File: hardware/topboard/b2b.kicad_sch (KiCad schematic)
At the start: 50 parts

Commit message: Add IMU
Signed-off-by: gatecat <gatecat@ds0.me>
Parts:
- removed C? (x4): 100n, symbol Device:C_Small
- added C? (x4): 100n, symbol Device:C_Small
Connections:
- net GTR_LEFT_C2M+: now also JL.B20
- net GTR_LEFT_C2M-: now also JL.B21
- net GTR_LEFT_M2C+: now also JL.B23
- net GTR_LEFT_M2C-: now also JL.B24
- net GTR_RIGHT_C2M+: now also C?.2; no longer JL?.B23
- net GTR_RIGHT_C2M-: now also C?.2; no longer JL?.B24
- net GTR_RIGHT_M2C+: now also C?.2; no longer JL?.B20
- net GTR_RIGHT_M2C-: now also C?.2; no longer JL?.B21
- new net: C?.1, JL?.B20
- new net: C?.1, JL?.B21
- new net: C?.1, JL?.B23
- new net: C?.1, JL?.B24

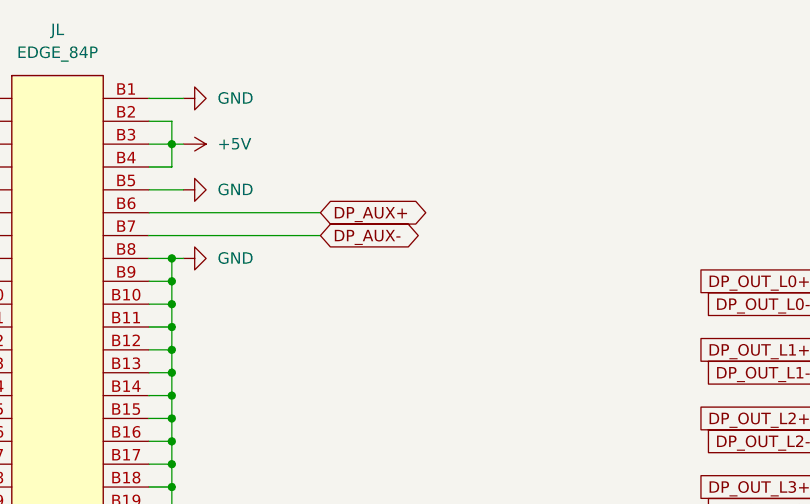
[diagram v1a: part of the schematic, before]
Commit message: Connecting some misc SoM IO
Signed-off-by: gatecat <gatecat@ds0.me>
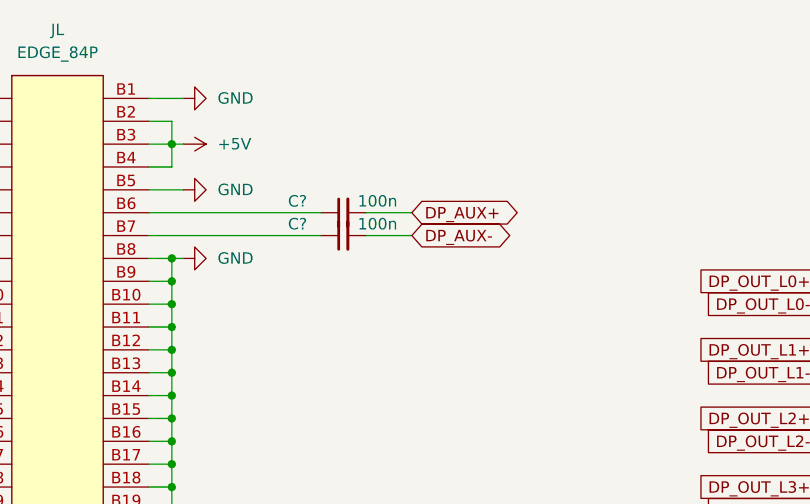
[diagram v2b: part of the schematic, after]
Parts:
- added C? (x2): 100n, symbol Device:C_Small
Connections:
- net DP_AUX+: now also C?.2; no longer JL.B6
- net DP_AUX-: now also C?.2; no longer JL.B7
- new net: C?.1, JL.B7
- new net: C?.1, JL.B6
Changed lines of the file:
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@@
     (stroke (width 0) (type default) (color 0 0 0 0))
   )
+  (wire (pts (xy 96.52 39.37) (xy 101.6 39.37))
+    (stroke (width 0) (type default) (color 0 0 0 0))
+  )
+  (wire (pts (xy 96.52 41.91) (xy 101.6 41.91))
+    (stroke (width 0) (type default) (color 0 0 0 0))
+  )
   (wire (pts (xy 109.22 130.81) (xy 72.39 130.81))
     (stroke (width 0) (type default) (color 0 0 0 0))
@@
     )
   )
-  (global_label "DP_AUX+" (shape bidirectional) (at 91.44 39.37 0) (fields_autoplaced)
+  (global_label "DP_AUX+" (shape bidirectional) (at 101.6 39.37 0) (fields_autoplaced)
     (effects (font (size 1.27 1.27)) (justify left))
-    (property "Intersheet References" "${INTERSHEET_REFS}" (id 0) (at 102.5617 39.2906 0)
+    (property "Intersheet References" "${INTERSHEET_REFS}" (id 0) (at 112.7217 39.2906 0)
       (effects (font (size 1.27 1.27)) (justify left) hide)
     )
   )
-  (global_label "DP_AUX-" (shape bidirectional) (at 91.44 41.91 0) (fields_autoplaced)
+  (global_label "DP_AUX-" (shape bidirectional) (at 101.6 41.91 0) (fields_autoplaced)
     (effects (font (size 1.27 1.27)) (justify left))
-    (property "Intersheet References" "${INTERSHEET_REFS}" (id 0) (at 102.5617 41.8306 0)
+    (property "Intersheet References" "${INTERSHEET_REFS}" (id 0) (at 112.7217 41.8306 0)
       (effects (font (size 1.27 1.27)) (justify left) hide)
     )
@@
       (effects (font (size 1.27 1.27)) hide)
     )
+    (pin "1")
+    (pin "2")
+  )
+  (symbol (lib_id "Device:C_Small") (at 93.98 39.37 90) (unit 1)
+    (in_bom yes) (on_board yes)
+    (property "Reference" "C?" (id 0) (at 88.9 38.1 90))
+    (property "Value" "100n" (id 1) (at 97.79 38.1 90))
+    (property "Footprint" "" (id 2) (at 93.98 39.37 0)
+      (effects (font (size 1.27 1.27)) hide)
+    )
+    (property "Datasheet" "~" (id 3) (at 93.98 39.37 0)
+      (effects (font (size 1.27 1.27)) hide)
+    )
+    (pin "1")
+    (pin "2")
+  )
+  (symbol (lib_id "Device:C_Small") (at 93.98 41.91 90) (unit 1)
+    (in_bom yes) (on_board yes)
+    (property "Reference" "C?" (id 0) (at 88.9 40.64 90))
+    (property "Value" "100n" (id 1) (at 97.79 40.64 90))
+    (property "Footprint" "" (id 2) (at 93.98 41.91 0)
+      (effects (font (size 1.27 1.27)) hide)
+    )
+    (property "Datasheet" "~" (id 3) (at 93.98 41.91 0)
+      (effects (font (size 1.27 1.27)) hide)
+    )

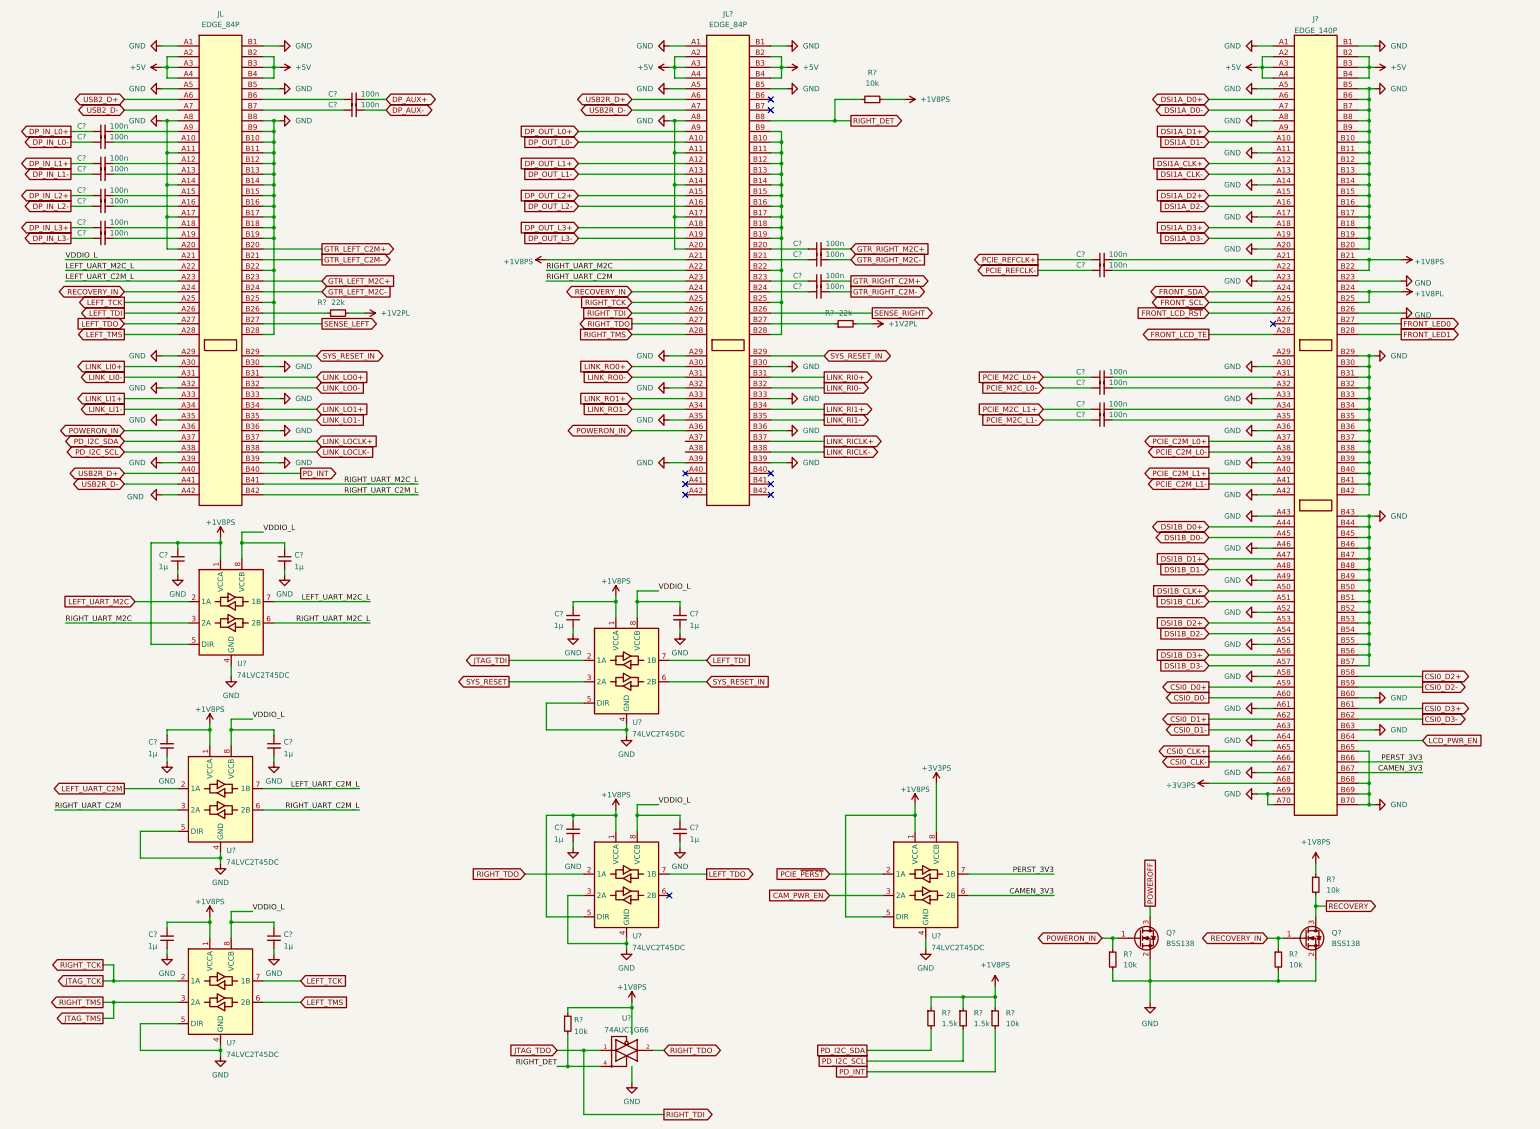
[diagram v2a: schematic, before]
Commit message: Fixing various top board issues
Signed-off-by: gatecat <gatecat@ds0.me>
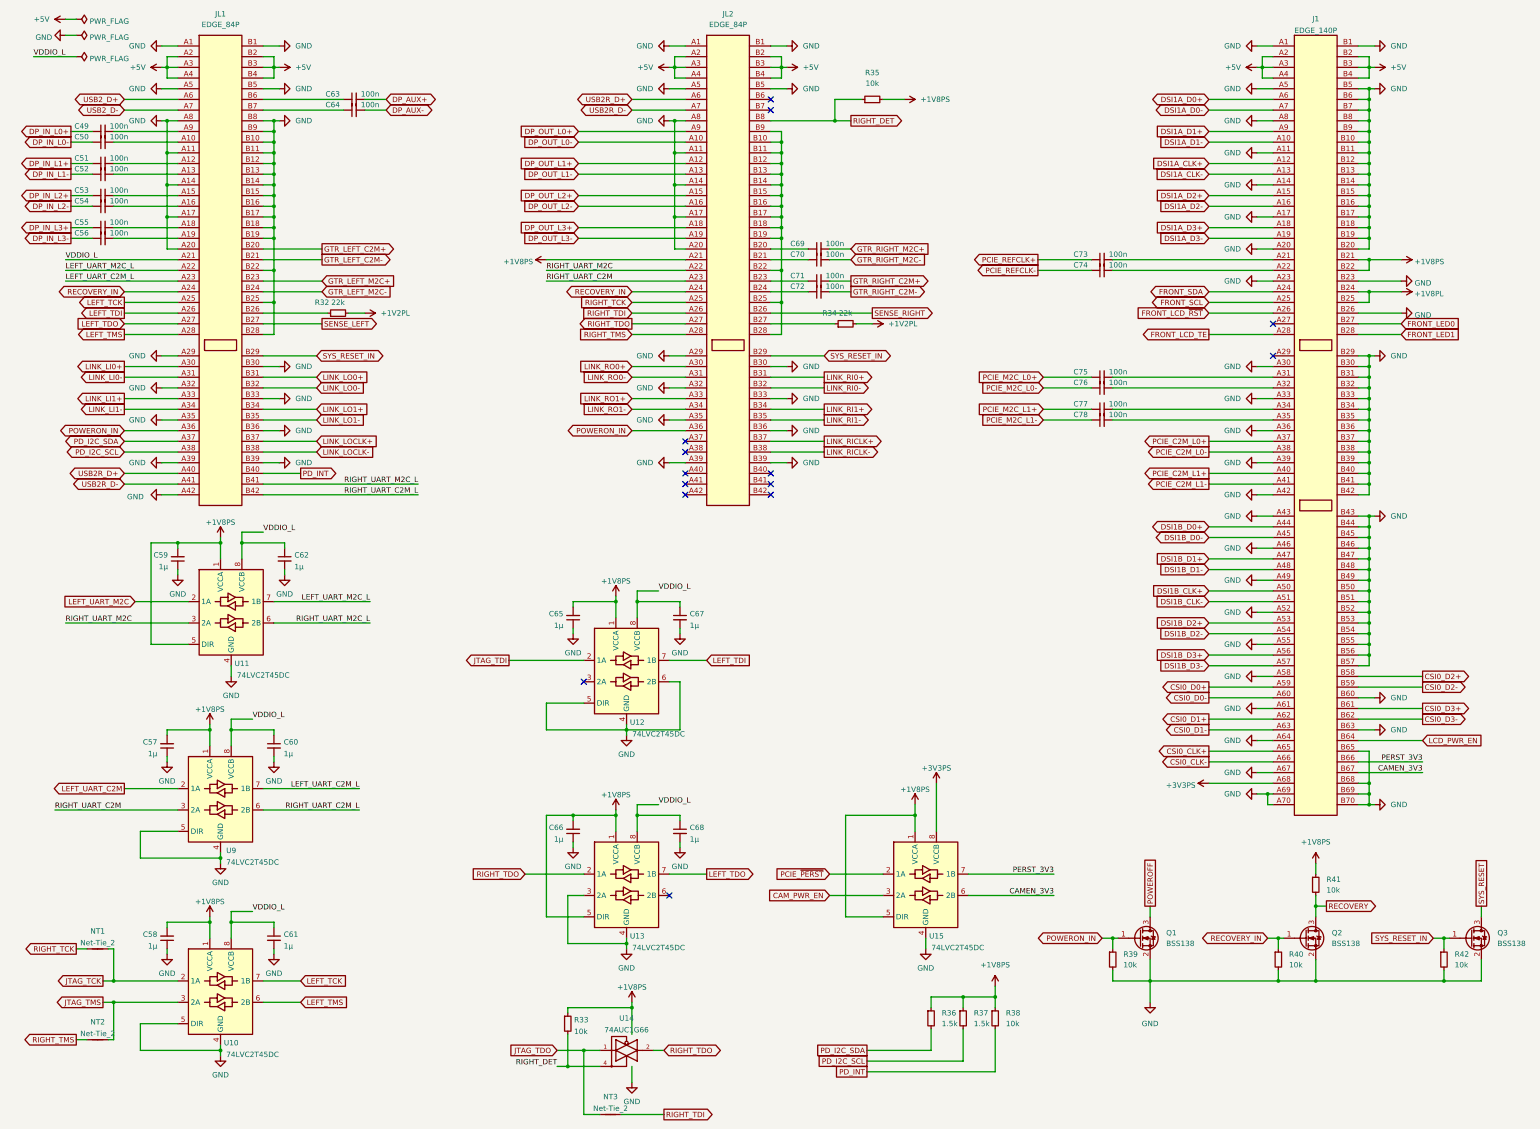
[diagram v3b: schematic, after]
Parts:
- added NT1, NT2, NT3: Net-Tie_2, symbol Device:Net-Tie_2
- added Q3: BSS138, Package_TO_SOT_SMD:SOT-23, symbol Transistor_FET:BSS138
- added R42: 10k, symbol Device:R_Small
- gave numbers to parts that had none: 51
- renumbered JL to JL1
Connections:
- net GND: now also U12.6 (2B), Q3.2 (S), R42.2
- net JTAG_TCK: now also NT1.2; no longer JL2.A25
- net JTAG_TDO: now also NT3.1; no longer JL2.A26
- net JTAG_TMS: now also NT2.2; no longer JL2.A28
- net SYS_RESET: now also Q3.3 (D); no longer U12.3 (2A)
- net SYS_RESET_IN: now also Q3.1 (G), R42.1; no longer U12.6 (2B)
- new net RIGHT_TCK: JL2.A25, NT1.1
- new net RIGHT_TDI: JL2.A26, NT3.2
- new net RIGHT_TMS: JL2.A28, NT2.1
- no-connect marks 10 -> 14

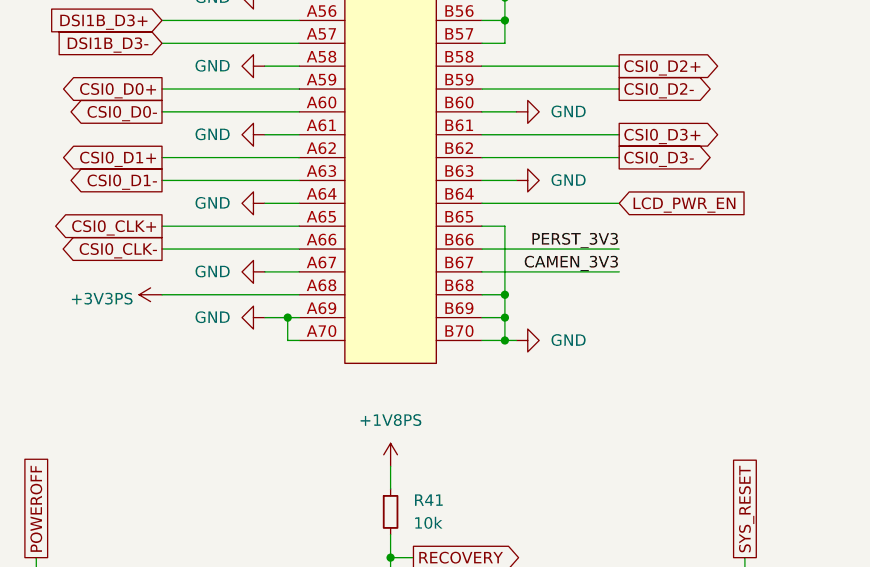
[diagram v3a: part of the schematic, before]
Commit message: Fixing various front and top board issues
Signed-off-by: gatecat <gatecat@ds0.me>
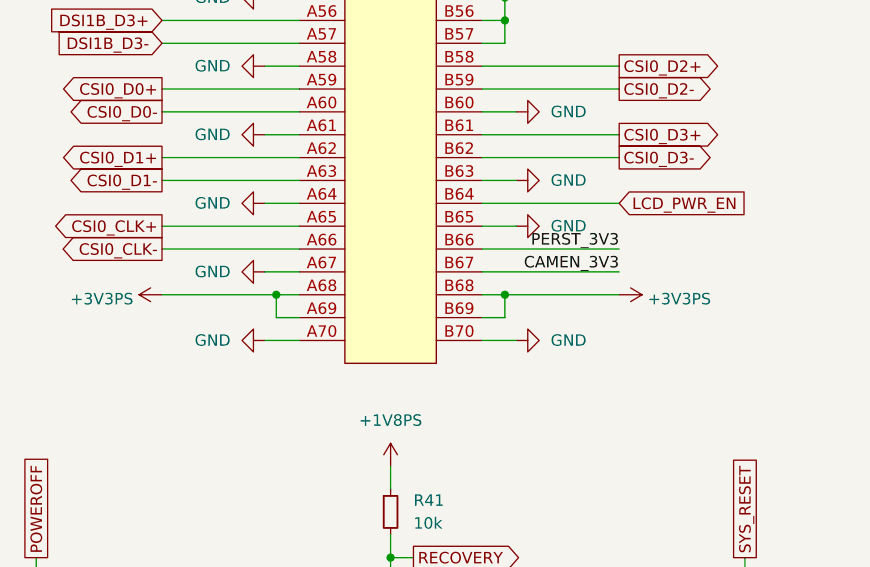
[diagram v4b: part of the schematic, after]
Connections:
- net +3V3PS: now also J1.A69, J1.B68, J1.B69
- net GND: no longer J1.A69, J1.B68, J1.B69
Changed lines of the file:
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@@
   (junction (at 283.21 248.92) (diameter 0) (color 0 0 0 0))
   (junction (at 309.88 31.75) (diameter 0) (color 0 0 0 0))
-  (junction (at 311.15 204.47) (diameter 0) (color 0 0 0 0))
+  (junction (at 309.88 201.93) (diameter 0) (color 0 0 0 0))
   (junction (at 313.69 238.76) (diameter 0) (color 0 0 0 0))
   (junction (at 313.69 248.92) (diameter 0) (color 0 0 0 0))
@@
   (junction (at 335.28 171.45) (diameter 0) (color 0 0 0 0))
   (junction (at 335.28 201.93) (diameter 0) (color 0 0 0 0))
-  (junction (at 335.28 204.47) (diameter 0) (color 0 0 0 0))
-  (junction (at 335.28 207.01) (diameter 0) (color 0 0 0 0))
   (junction (at 353.06 238.76) (diameter 0) (color 0 0 0 0))
   (junction (at 353.06 248.92) (diameter 0) (color 0 0 0 0))
@@
     (stroke (width 0) (type default) (color 0 0 0 0))
   )
-  (wire (pts (xy 297.18 201.93) (xy 312.42 201.93))
+  (wire (pts (xy 297.18 201.93) (xy 309.88 201.93))
     (stroke (width 0) (type default) (color 0 0 0 0))
   )
@@
     (stroke (width 0) (type default) (color 0 0 0 0))
   )
-  (wire (pts (xy 308.61 204.47) (xy 311.15 204.47))
+  (wire (pts (xy 308.61 207.01) (xy 312.42 207.01))
     (stroke (width 0) (type default) (color 0 0 0 0))
   )
@@
     (stroke (width 0) (type default) (color 0 0 0 0))
   )
-  (wire (pts (xy 311.15 204.47) (xy 312.42 204.47))
+  (wire (pts (xy 309.88 201.93) (xy 312.42 201.93))
     (stroke (width 0) (type default) (color 0 0 0 0))
   )
-  (wire (pts (xy 311.15 207.01) (xy 311.15 204.47))
+  (wire (pts (xy 309.88 204.47) (xy 309.88 201.93))
     (stroke (width 0) (type default) (color 0 0 0 0))
   )
@@
     (stroke (width 0) (type default) (color 0 0 0 0))
   )
-  (wire (pts (xy 312.42 207.01) (xy 311.15 207.01))
+  (wire (pts (xy 312.42 204.47) (xy 309.88 204.47))
     (stroke (width 0) (type default) (color 0 0 0 0))
   )
@@
     (stroke (width 0) (type default) (color 0 0 0 0))
   )
+  (wire (pts (xy 332.74 194.31) (xy 336.55 194.31))
+    (stroke (width 0) (type default) (color 0 0 0 0))
+  )
   (wire (pts (xy 332.74 196.85) (xy 347.98 196.85))
     (stroke (width 0) (type default) (color 0 0 0 0))
@@
     (stroke (width 0) (type default) (color 0 0 0 0))
   )
-  (wire (pts (xy 332.74 207.01) (xy 335.28 207.01))
+  (wire (pts (xy 332.74 207.01) (xy 336.55 207.01))
     (stroke (width 0) (type default) (color 0 0 0 0))
   )
@@
     (stroke (width 0) (type default) (color 0 0 0 0))
   )
-  (wire (pts (xy 335.28 194.31) (xy 332.74 194.31))
-    (stroke (width 0) (type default) (color 0 0 0 0))
-  )
   (wire (pts (xy 335.28 201.93) (xy 332.74 201.93))
     (stroke (width 0) (type default) (color 0 0 0 0))
   )
-  (wire (pts (xy 335.28 201.93) (xy 335.28 194.31))
+  (wire (pts (xy 335.28 201.93) (xy 347.98 201.93))
     (stroke (width 0) (type default) (color 0 0 0 0))
   )
@@
     (stroke (width 0) (type default) (color 0 0 0 0))
   )
-  (wire (pts (xy 335.28 204.47) (xy 335.28 207.01))
-    (stroke (width 0) (type default) (color 0 0 0 0))
-  )
-  (wire (pts (xy 335.28 207.01) (xy 336.55 207.01))
-    (stroke (width 0) (type default) (color 0 0 0 0))
-  )
   (wire (pts (xy 336.55 26.67) (xy 332.74 26.67))
     (stroke (width 0) (type default) (color 0 0 0 0))
@@
     (pin "1")
   )
+  (symbol (lib_id "meowality:+3V3PS") (at 347.98 201.93 270) (unit 1)
+    (in_bom yes) (on_board yes) (fields_autoplaced)
+    (property "Reference" "#PWR?" (id 0) (at 344.17 201.93 0)
+      (effects (font (size 1.27 1.27)) hide)
+    )
+    (property "Value" "+3V3PS" (id 1) (at 351.155 202.409 90)
+      (effects (font (size 1.27 1.27)) (justify left))
+    )
+    (property "Footprint" "" (id 2) (at 347.98 201.93 0)
+      (effects (font (size 1.27 1.27)) hide)
+    )
+    (property "Datasheet" "" (id 3) (at 347.98 201.93 0)
+      (effects (font (size 1.27 1.27)) hide)
+    )
+    (pin "1")
+  )
   (symbol (lib_id "Device:Net-Tie_2") (at 33.02 241.3 0) (unit 1)
     (in_bom yes) (on_board yes) (fields_autoplaced)
@@
     (pin "1")
   )
-  (symbol (lib_id "power:GND") (at 308.61 204.47 270) (unit 1)
+  (symbol (lib_id "power:GND") (at 308.61 207.01 270) (unit 1)
     (in_bom yes) (on_board yes) (fields_autoplaced)
-    (property "Reference" "#PWR0342" (id 0) (at 302.26 204.47 0)
+    (property "Reference" "#PWR0342" (id 0) (at 302.26 207.01 0)
       (effects (font (size 1.27 1.27)) hide)
     )
-    (property "Value" "GND" (id 1) (at 304.8 204.4699 90)
+    (property "Value" "GND" (id 1) (at 304.8 207.0099 90)
       (effects (font (size 1.27 1.27)) (justify right))
     )
-    (property "Footprint" "" (id 2) (at 308.61 204.47 0)
+    (property "Footprint" "" (id 2) (at 308.61 207.01 0)
       (effects (font (size 1.27 1.27)) hide)
     )
-    (property "Datasheet" "" (id 3) (at 308.61 204.47 0)
+    (property "Datasheet" "" (id 3) (at 308.61 207.01 0)
       (effects (font (size 1.27 1.27)) hide)
     )
@@
       (effects (font (size 1.27 1.27)) hide)
     )
+    (pin "1")
+  )
+  (symbol (lib_id "power:GND") (at 336.55 194.31 90) (unit 1)
+    (in_bom yes) (on_board yes) (fields_autoplaced)
+    (property "Reference" "#PWR?" (id 0) (at 342.9 194.31 0)
+      (effects (font (size 1.27 1.27)) hide)
+    )
+    (property "Value" "GND" (id 1) (at 340.36 194.3101 90)
+      (effects (font (size 1.27 1.27)) (justify right))
+    )
+    (property "Footprint" "" (id 2) (at 336.55 194.31 0)
+      (effects (font (size 1.27 1.27)) hide)
+    )
+    (property "Datasheet" "" (id 3) (at 336.55 194.31 0)
+      (effects (font (size 1.27 1.27)) hide)
+    )

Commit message: Assign most top-board footprints
Signed-off-by: gatecat <gatecat@ds0.me>
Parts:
- C49, C50, C51, C52, C53, C54, C55, C56, C63, C64, C69, C70, C71, C72, C73, C74, C75, C76, C77, C78: footprint (none) -> Capacitor_SMD:C_0402_1005Metric
- C57, C58, C59, C60, C61, C62, C65, C66, C67, C68: footprint (none) -> Capacitor_SMD:C_0603_1608Metric
- J1: footprint (none) -> meowality:ME1014010101011
- JL1: footprint (none) -> meowality:MET008431401101
- JL2: footprint (none) -> meowality:EDGE_84P_0.6mm
- NT1, NT2, NT3: footprint (none) -> NetTie:NetTie-2_SMD_Pad0.5mm
- R32, R33, R34, R35, R36, R37, R38, R39, R40, R41, R42: footprint (none) -> Resistor_SMD:R_0402_1005Metric
- U10, U11, U12, U13, U15, U9: footprint Package_SO:VSSOP-8_2.3x2mm_P0.5mm -> Package_SON:X2SON-8_1.4x1mm_P0.35mm
- U14: footprint (none) -> Package_TO_SOT_SMD:SOT-23-5
